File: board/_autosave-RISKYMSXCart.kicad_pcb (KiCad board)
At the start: 4 copper layers, 71.9 x 55.5 mm, 35 parts, among them CN1 MSX_CART, IC1 LM1117MPX-3.3, J1 Conn_01x02, J2 Conn_01x02, J7 USB_1, J8 Conn_01x02, SW1 SW_Push, U1 CH32V307VCT6, U3 NE5532

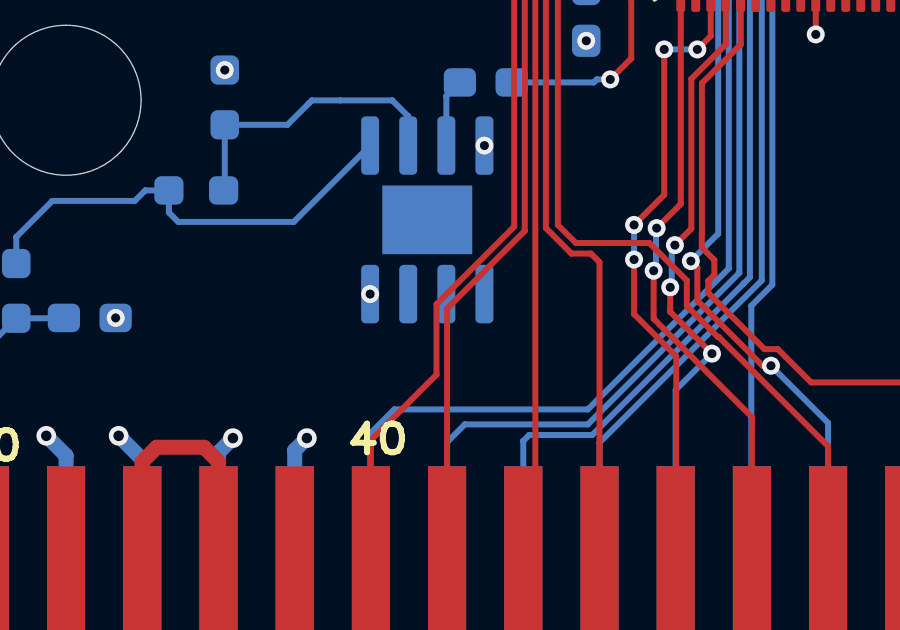
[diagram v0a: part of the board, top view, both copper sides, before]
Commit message: scc experimentation with tiimings modes adn DMA use
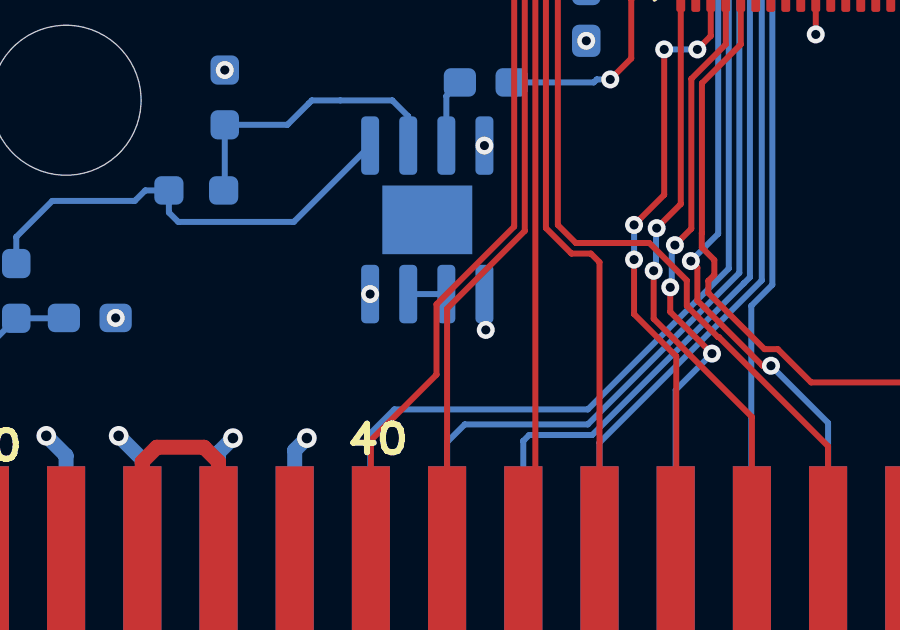
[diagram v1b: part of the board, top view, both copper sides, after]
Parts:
- C1: value 100nF -> 10uF
- C3: value 10uF -> 100nF
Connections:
- U3 pad 5: unconnected-(U3B-+-Pad5) -> GND
- U3 pad 6: unconnected-(U3B---Pad6) -> Net-(U3B--)
- U3 pad 7: unconnected-(U3-Pad7) -> Net-(U3B--)
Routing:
- net Net-(U3B--): track 0.00 -> 1.27 mm
- net GND: track 33.3 -> 34.5 mm, vias 26 -> 27
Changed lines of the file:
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@@
 	(net 100 "unconnected-(U1-OSC_OUT-Pad13)")
 	(net 101 "/LED")
-	(net 102 "unconnected-(U3-Pad7)")
-	(net 103 "unconnected-(U3B---Pad6)")
-	(net 104 "unconnected-(U3B-+-Pad5)")
+	(net 102 "Net-(U3B--)")
 	(footprint "Connector_PinHeader_2.54mm:PinHeader_1x02_P2.54mm_Vertical"
 		(layer "F.Cu")
@@
 		(sheetname "/")
 		(sheetfile "RISKYMSXCart.kicad_sch")
-		(attr through_hole)
+		(attr through_hole exclude_from_bom)
 		(fp_line
 			(start -1.33 -1.33)
@@
 		(sheetname "/")
 		(sheetfile "RISKYMSXCart.kicad_sch")
-		(attr smd)
+		(attr smd exclude_from_bom)
 		(fp_line
 			(start 3.1 -1.3)
@@
 		(sheetname "/")
 		(sheetfile "RISKYMSXCart.kicad_sch")
-		(attr through_hole)
+		(attr through_hole exclude_from_bom)
 		(fp_line
 			(start -1.33 3.87)
@@
 		(sheetname "/")
 		(sheetfile "RISKYMSXCart.kicad_sch")
-		(attr smd)
+		(attr smd exclude_from_bom)
 		(fp_line
 			(start -1.86 0.96)
@@
 			)
 		)
-		(property "Datasheet" " ~"
+		(property "Datasheet" ""
 			(at 0 0 180)
 			(unlocked yes)
@@
 		(sheetname "/")
 		(sheetfile "RISKYMSXCart.kicad_sch")
-		(attr through_hole)
+		(attr through_hole exclude_from_bom)
 		(fp_line
 			(start 10.86 0.86)
@@
 		(sheetname "/")
 		(sheetfile "RISKYMSXCart.kicad_sch")
-		(attr through_hole)
+		(attr through_hole exclude_from_bom)
 		(fp_line
 			(start 1.33 1.27)
@@
 		(sheetname "/")
 		(sheetfile "RISKYMSXCart.kicad_sch")
+		(attr exclude_from_bom)
 		(pad "P1" smd rect
 			(at 63.5 -5.08 180)
@@
 		(sheetname "/")
 		(sheetfile "RISKYMSXCart.kicad_sch")
-		(attr smd)
+		(attr smd exclude_from_bom)
 		(fp_line
 			(start -1.86 0.96)
@@
 		(sheetname "/")
 		(sheetfile "RISKYMSXCart.kicad_sch")
-		(attr smd)
+		(attr smd exclude_from_bom)
 		(fp_line
 			(start 7.11 -7.11)
@@
 			)
 		)
+		(property "LCSC Part #" "C22962"
+			(at 0 0 270)
+			(unlocked yes)
+			(layer "B.Fab")
+			(hide yes)
+			(effects
+				(font
+					(size 1 1)
+					(thickness 0.15)
+				)
+				(justify mirror)
+			)
+		)
 		(property ki_fp_filters "R_*")
 		(sheetname "/")
@@
 			)
 		)
+		(property "LCSC Part #" "C9196"
+			(at 0 0 0)
+			(unlocked yes)
+			(layer "B.Fab")
+			(hide yes)
+			(effects
+				(font
+					(size 1 1)
+					(thickness 0.15)
+				)
+				(justify mirror)
+			)
+		)
 		(sheetname "/")
 		(sheetfile "RISKYMSXCart.kicad_sch")
@@
 			)
 		)
-		(property "Value" "100nF"
+		(property "Value" "10uF"
 			(at -1.27 -2.54 90)
 			(layer "B.Fab")
@@
 			)
 		)
+		(property "LCSC Part #" "C70462"
+			(at 0 0 270)
+			(unlocked yes)
+			(layer "B.Fab")
+			(hide yes)
+			(effects
+				(font
+					(size 1 1)
+					(thickness 0.15)
+				)
+				(justify mirror)
+			)
+		)
 		(sheetname "/")
 		(sheetfile "RISKYMSXCart.kicad_sch")
@@
 			)
 		)
-		(property "LCSC Part #" ""
+		(property "LCSC Part #" "C9196"
 			(at 0 0 180)
 			(unlocked yes)
@@
 			)
 		)
+		(property "LCSC Part #" "C6186"
+			(at 0 0 180)
+			(unlocked yes)
+			(layer "B.Fab")
+			(hide yes)
+			(effects
+				(font
+					(size 1 1)
+					(thickness 0.15)
+				)
+				(justify mirror)
+			)
+		)
 		(sheetname "/")
 		(sheetfile "RISKYMSXCart.kicad_sch")
@@
 			)
 		)
+		(property "LCSC Part #" "C21190"
+			(at 0 0 270)
+			(unlocked yes)
+			(layer "B.Fab")
+			(hide yes)
+			(effects
+				(font
+					(size 1 1)
+					(thickness 0.15)
+				)
+				(justify mirror)
+			)
+		)
 		(property ki_fp_filters "R_*")
 		(sheetname "/")
@@
 			)
 		)
+		(property "LCSC Part #" "C22962"
+			(at 0 0 90)
+			(unlocked yes)
+			(layer "B.Fab")
+			(hide yes)
+			(effects
+				(font
+					(size 1 1)
+					(thickness 0.15)
+				)
+				(justify mirror)
+			)
+		)
 		(sheetname "/")
 		(sheetfile "RISKYMSXCart.kicad_sch")
@@
 			)
 		)
+		(property "LCSC Part #" "C57112"
+			(at 0 0 0)
+			(unlocked yes)
+			(layer "B.Fab")
+			(hide yes)
+			(effects
+				(font
+					(size 1 1)
+					(thickness 0.15)
+				)
+				(justify mirror)
+			)
+		)
 		(property ki_fp_filters "C_*")
 		(sheetname "/")
@@
 			)
 		)
+		(property "LCSC Part #" "C1705"
+			(at 0 0 180)
+			(unlocked yes)
+			(layer "B.Fab")
+			(hide yes)
+			(effects
+				(font
+					(size 1 1)
+					(thickness 0.15)
+				)
+				(justify mirror)
+			)
+		)
 		(property ki_fp_filters "C_*")
 		(sheetname "/")
@@
 			)
 		)
-		(property "Value" "10uF"
+		(property "Value" "100nF"
 			(at -0.635 -1.905 0)
 			(layer "B.Fab")
@@
 			)
 		)
+		(property "LCSC Part #" "C1588"
+			(at 0 0 180)
+			(unlocked yes)
+			(layer "B.Fab")
+			(hide yes)
+			(effects
+				(font
+					(size 1 1)
+					(thickness 0.15)
+				)
+				(justify mirror)
+			)
+		)
 		(sheetname "/")
 		(sheetfile "RISKYMSXCart.kicad_sch")
@@
 			)
 		)
+		(property "LCSC Part #" "C7426"
+			(at 0 0 270)
+			(unlocked yes)
+			(layer "B.Fab")
+			(hide yes)
+			(effects
+				(font
+					(size 1 1)
+					(thickness 0.15)
+				)
+				(justify mirror)
+			)
+		)
 		(property ki_fp_filters "SOIC*3.9x4.9mm*P1.27mm* DIP*W7.62mm* TO*99* OnSemi*Micro8* TSSOP*3x3mm*P0.65mm* TSSOP*4.4x3mm*P0.65mm* MSOP*3x3mm*P0.65mm* SSOP*3.9x4.9mm*P0.635mm* LFCSP*2x2mm*P0.5mm* *SIP* SOIC*5.3x6.2mm*P1.27mm*")
 		(sheetname "/")
@@
 			(layers "B.Cu" "B.Mask" "B.Paste")
 			(roundrect_rratio 0.25)
-			(net 104 "unconnected-(U3B-+-Pad5)")
+			(net 1 "GND")
 			(pinfunction "+")
-			(pintype "input+no_connect")
+			(pintype "input")
 		)
 		(pad "6" smd roundrect
@@
 			(layers "B.Cu" "B.Mask" "B.Paste")
 			(roundrect_rratio 0.25)
-			(net 103 "unconnected-(U3B---Pad6)")
+			(net 102 "Net-(U3B--)")
 			(pinfunction "-")
-			(pintype "input+no_connect")
+			(pintype "input")
 		)
 		(pad "7" smd roundrect
@@
 			(layers "B.Cu" "B.Mask" "B.Paste")
 			(roundrect_rratio 0.25)
-			(net 102 "unconnected-(U3-Pad7)")
-			(pintype "output+no_connect")
+			(net 102 "Net-(U3B--)")
+			(pintype "output")
 		)
 		(pad "8" smd roundrect
@@
 			)
 		)
+		(property "LCSC Part #" "C25804"
+			(at 0 0 270)
+			(unlocked yes)
+			(layer "B.Fab")
+			(hide yes)
+			(effects
+				(font
+					(size 1 1)
+					(thickness 0.15)
+				)
+				(justify mirror)
+			)
+		)
 		(property ki_fp_filters "R_*")
 		(sheetname "/")
@@
 	)
 	(via
+		(at 134.5 120.45)
+		(size 0.6)
+		(drill 0.3)
+		(layers "F.Cu" "B.Cu")
+		(free yes)
+		(net 1)
+	)
+	(via
 		(at 137.9 106.9)
 		(size 0.6)
@@
 	)
 	(segment
+		(start 134.5 120.45)
+		(end 134.5 119.3)
+		(width 0.2)
+		(layer "B.Cu")
+		(net 1)
+	)
+	(segment
 		(start 128.1303 124.462534)
 		(end 128.5367 124.056134)
@@
 	)
 	(segment
+		(start 134.5 119.3)
+		(end 134.455 119.255)
+		(width 0.2)
+		(layer "B.Cu")
+		(net 1)
+	)
+	(segment
 		(start 125.5903 124.538734)
 		(end 126.0729 124.056134)
@@
 		(net 101)
 	)
+	(segment
+		(start 133.185 119.255)
+		(end 131.915 119.255)
+		(width 0.2)
+		(layer "B.Cu")
+		(net 102)
+	)
 	(zone
